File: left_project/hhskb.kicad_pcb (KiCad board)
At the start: 2 copper layers, 141 x 118 mm, 90 parts, among them J1 4pin_Jack, SW1 SW_PUSH, SW11 SW_PUSH, SW12 SW_PUSH, SW13 SW_PUSH, SW14 SW_PUSH, SW15 SW_PUSH, SW16 SW_PUSH, SW17 SW_PUSH, SW21 SW_PUSH, SW22 SW_PUSH, SW23 SW_PUSH, SW24 SW_PUSH, SW25 SW_PUSH, SW26 SW_PUSH, SW31 SW_PUSH, SW32 SW_PUSH, SW33 SW_PUSH, SW34 SW_PUSH, SW35 SW_PUSH, SW36 SW_PUSH, SW41 SW_PUSH, SW42 SW_PUSH, SW43 SW_PUSH, SW44 SW_PUSH, SW45 SW_PUSH, SW46 SW_PUSH, SW51 SW_PUSH, SW52 SW_PUSH, SW53 SW_PUSH, SW54 SW_PUSH, SW55 SW_PUSH, SW56 SW_PUSH, U1 MCP23017

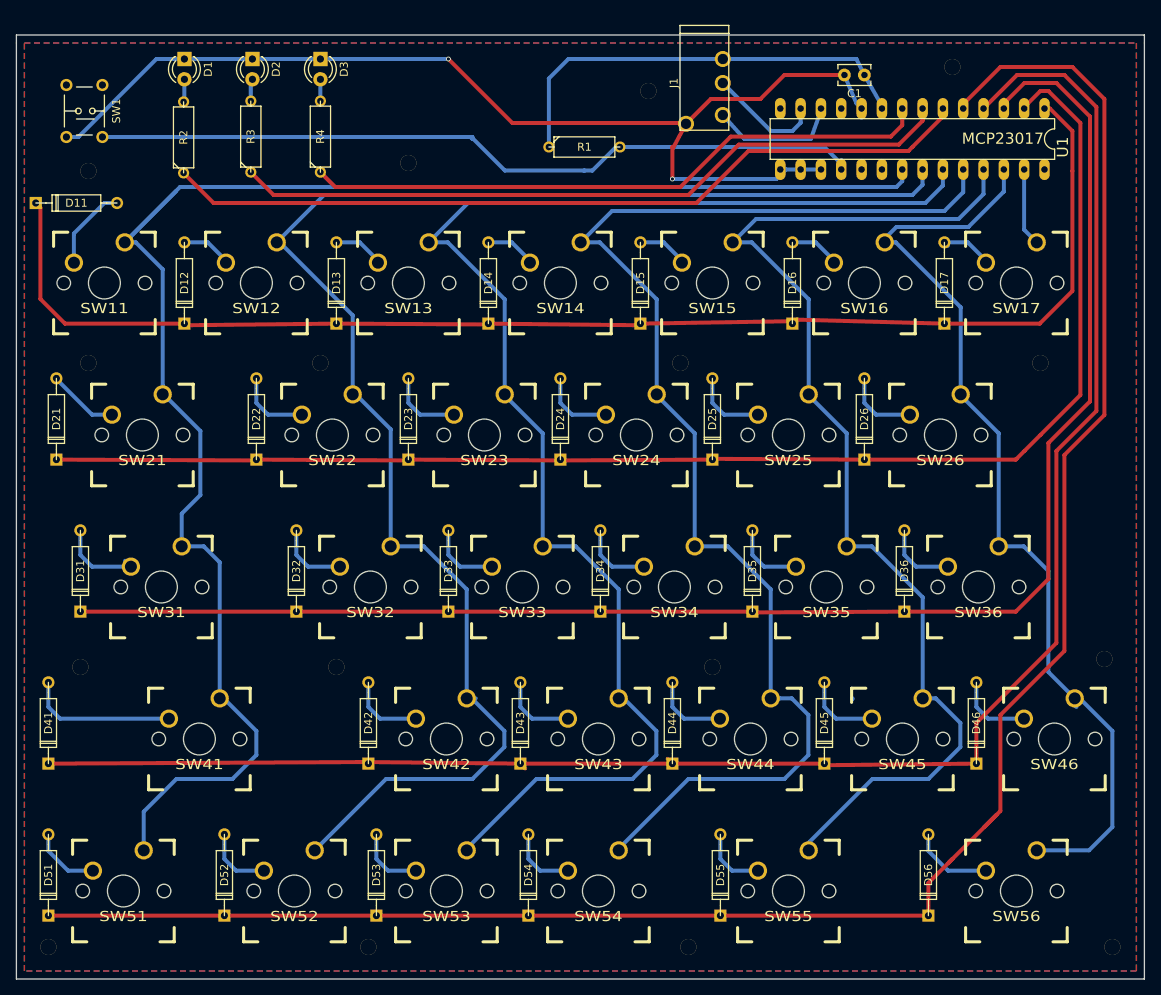
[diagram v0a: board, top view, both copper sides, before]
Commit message: 右手用で変更したライブラリを左に反映 左でしか使わないキーのサイズで穴をスルーホールに修正 ねじ穴をm2で2.5mm穴、レジスト付きに変更
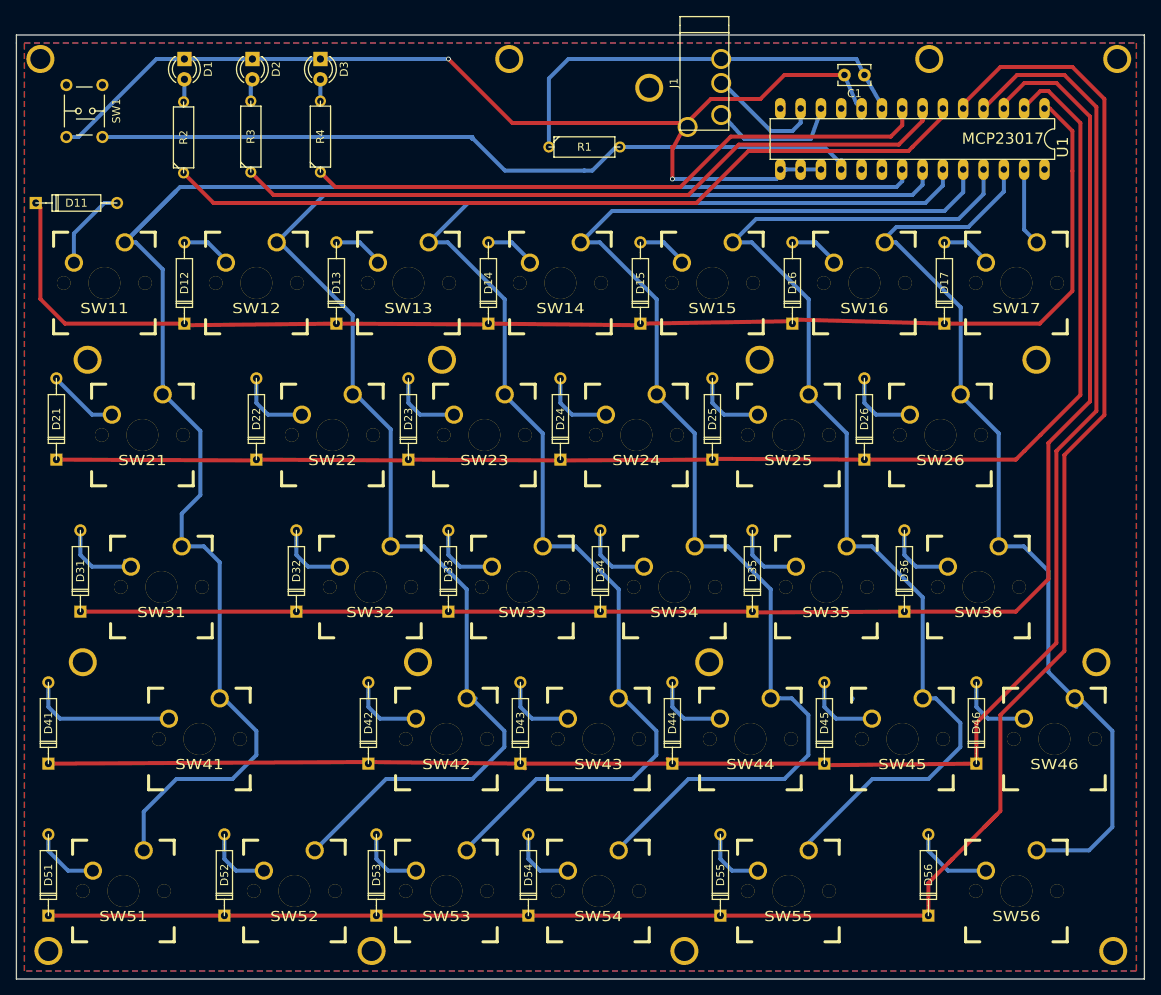
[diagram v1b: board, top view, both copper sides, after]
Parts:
- removed the ? at (116.0, 108.0)
- removed the ? at (38.0, 46.0)
- removed the ? at (161.0, 51.0)
- removed the ? at (33.0, 143.0)
- removed the ? at (37.0, 108.0)
- removed the ? at (38.0, 70.0)
- removed the ? at (108.0, 36.0)
- removed the ? at (146.0, 33.0)
- removed the ? at (113.0, 143.0)
- removed the ? at (157.0, 70.0)
- removed the ? at (67.0, 70.0)
- removed the ? at (112.0, 70.0)
- removed the ? at (69.0, 108.0)
- removed the ? at (165.0, 107.0)
- removed the ? at (73.0, 143.0)
- removed the ? at (166.0, 143.0)
- removed the ? at (78.0, 45.0)
- added ?: , MyFootprint:m2_neji_hole2.5_head3.5, F.Cu at (33.0, 143.5)
- added ?: , MyFootprint:m2_neji_hole2.5_head3.5, F.Cu at (82.2, 69.6)
- added ?: , MyFootprint:m2_neji_hole2.5_head3.5, F.Cu at (121.9, 69.6)
- added ?: , MyFootprint:m2_neji_hole2.5_head3.5, F.Cu at (156.5, 69.7)
- added ?: , MyFootprint:m2_neji_hole2.5_head3.5, F.Cu at (32.3, 32.3)
- added ?: , MyFootprint:m2_neji_hole2.5_head3.5, F.Cu at (90.6, 32.5)
- added ?: , MyFootprint:m2_neji_hole2.5_head3.5, F.Cu at (108.1, 35.6)
- added ?: , MyFootprint:m2_neji_hole2.5_head3.5, F.Cu at (143.1, 32.6)
- added ?: , MyFootprint:m2_neji_hole2.5_head3.5, F.Cu at (166.6, 32.6)
- added ?: , MyFootprint:m2_neji_hole2.5_head3.5, F.Cu at (73.4, 143.6)
- added ?: , MyFootprint:m2_neji_hole2.5_head3.5, F.Cu at (112.5, 143.0)
- added ?: , MyFootprint:m2_neji_hole2.5_head3.5, F.Cu at (166.1, 143.3)
- added ?: , MyFootprint:m2_neji_hole2.5_head3.5, F.Cu at (37.3, 107.1)
- added ?: , MyFootprint:m2_neji_hole2.5_head3.5, F.Cu at (79.2, 107.8)
- added ?: , MyFootprint:m2_neji_hole2.5_head3.5, F.Cu at (115.6, 107.6)
- added ?: , MyFootprint:m2_neji_hole2.5_head3.5, F.Cu at (164.0, 107.3)
- added ?: , MyFootprint:m2_neji_hole2.5_head3.5, F.Cu at (37.9, 69.6)
